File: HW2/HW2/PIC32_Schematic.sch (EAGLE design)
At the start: 22 parts

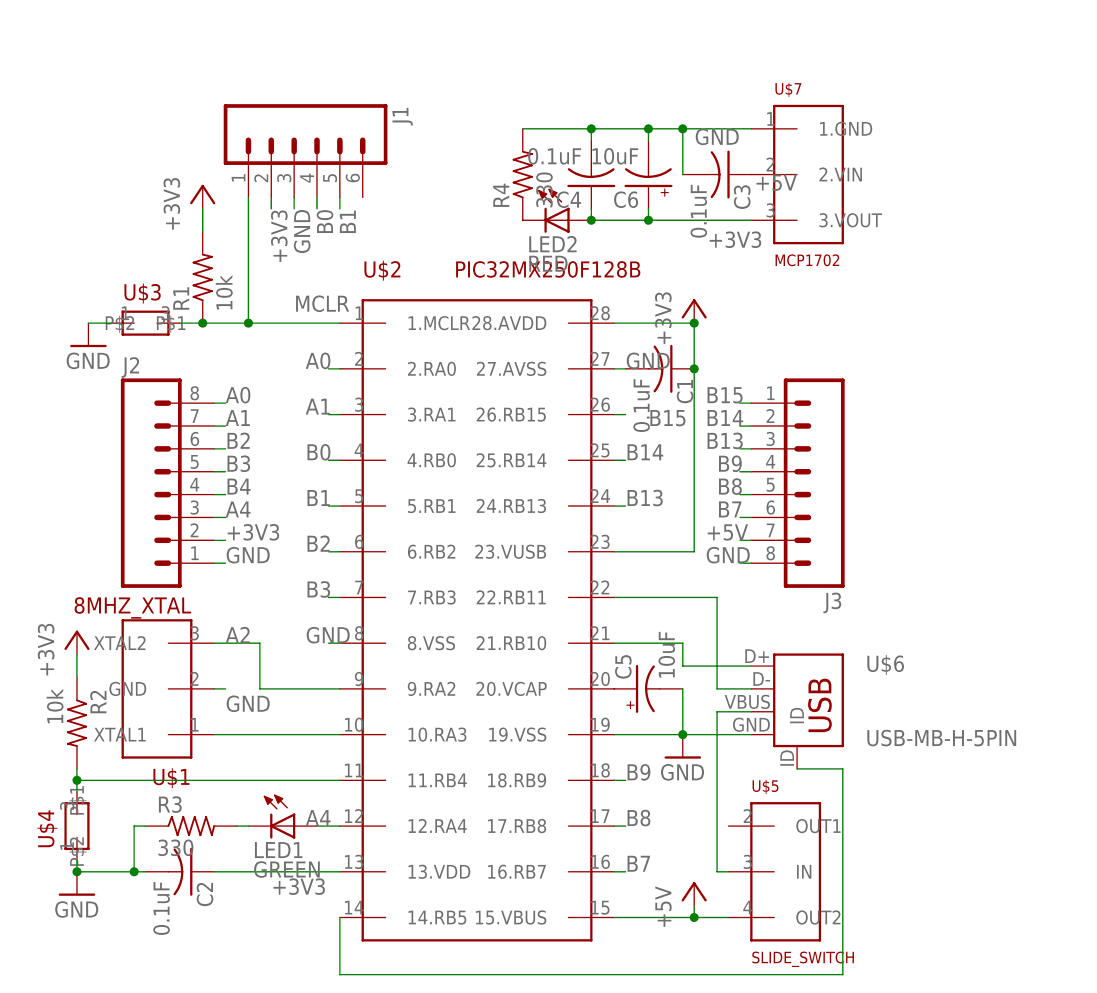
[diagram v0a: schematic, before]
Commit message: All components placed relative to each other
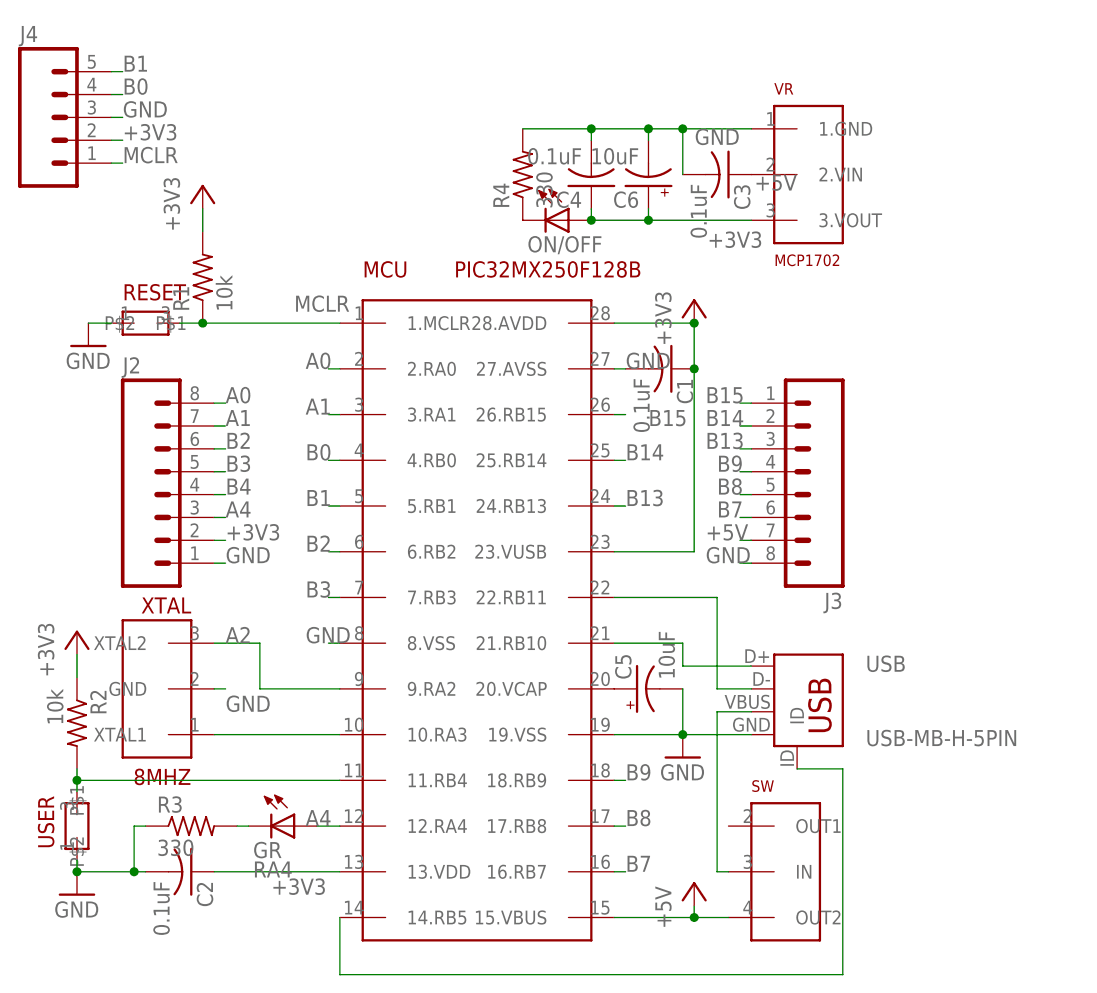
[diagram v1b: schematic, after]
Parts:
- removed J1: (no value), ME433:M06SILK_FEMALE_PTH
- added J4: (no value), ME433:M05PTH
- 8MHZ: value 8MHZ_XTAL -> XTAL
- GR: value GREEN -> RA4
- ON/OFF: value RED -> (none)
- renumbered LED1 to GR, LED2 to ON/OFF, U$1 to 8MHZ, U$2 to MCU, U$3 to RESET, U$4 to USER, U$5 to SW, U$6 to USB, U$7 to VR
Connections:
- net +3V3: now also J4.2; no longer J1.2
- net B0: now also J4.4; no longer J1.4
- net B1: now also J4.5; no longer J1.5
- net GND: now also J4.3; no longer J1.3
- net MCLR: now also J4.1; no longer J1.1
